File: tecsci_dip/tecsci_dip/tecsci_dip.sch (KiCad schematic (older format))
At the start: 0 parts

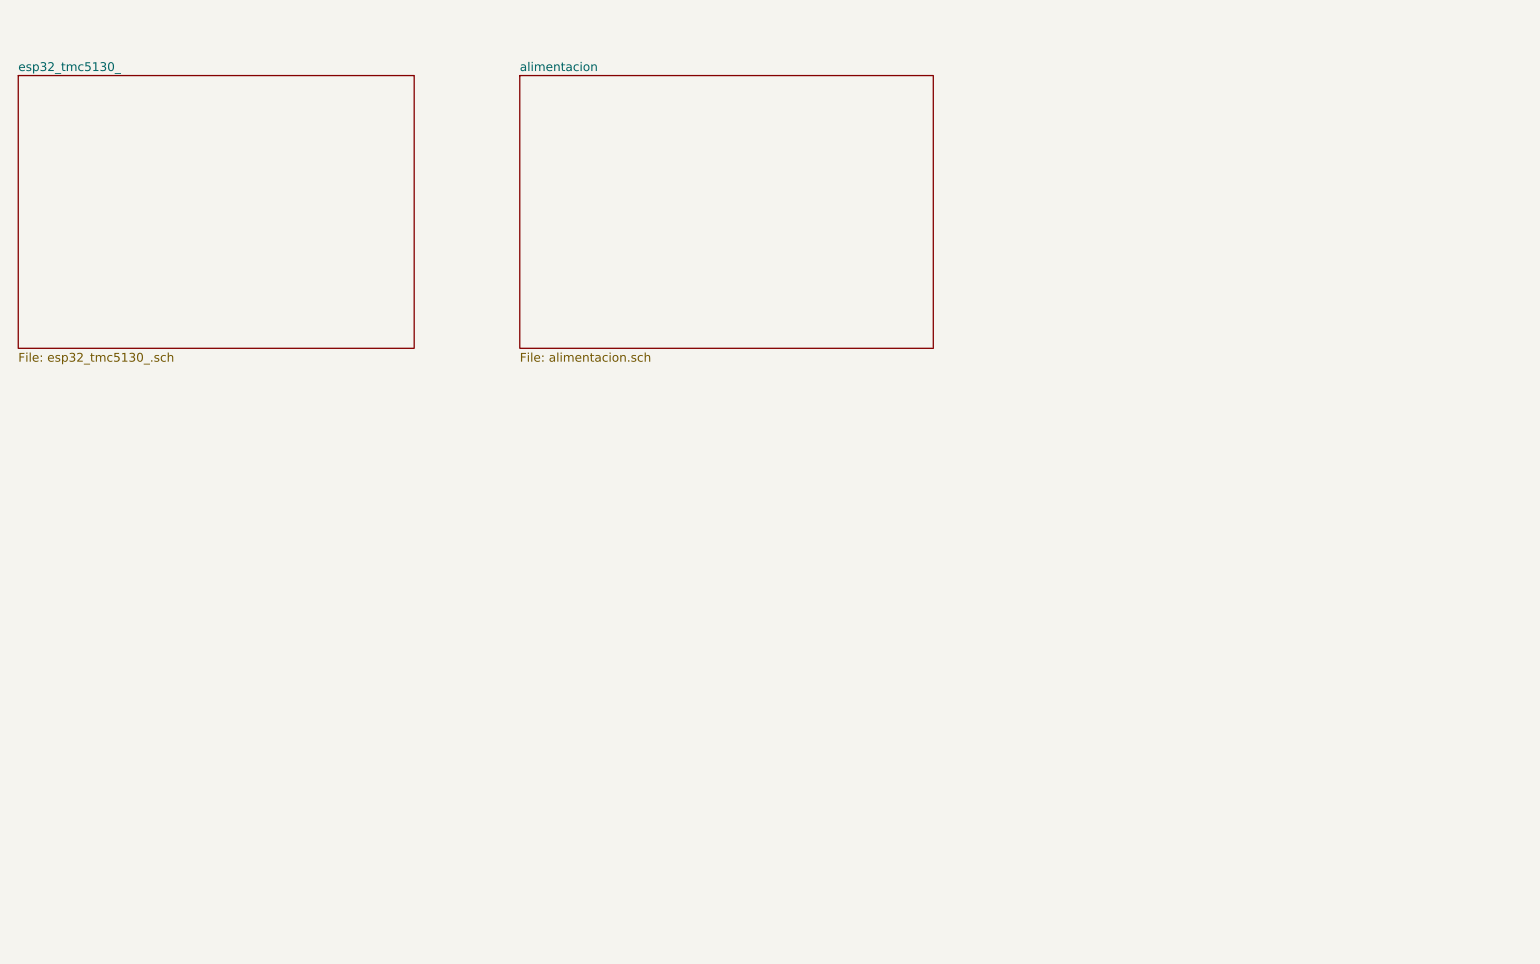
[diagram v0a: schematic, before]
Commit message: add value and footprint
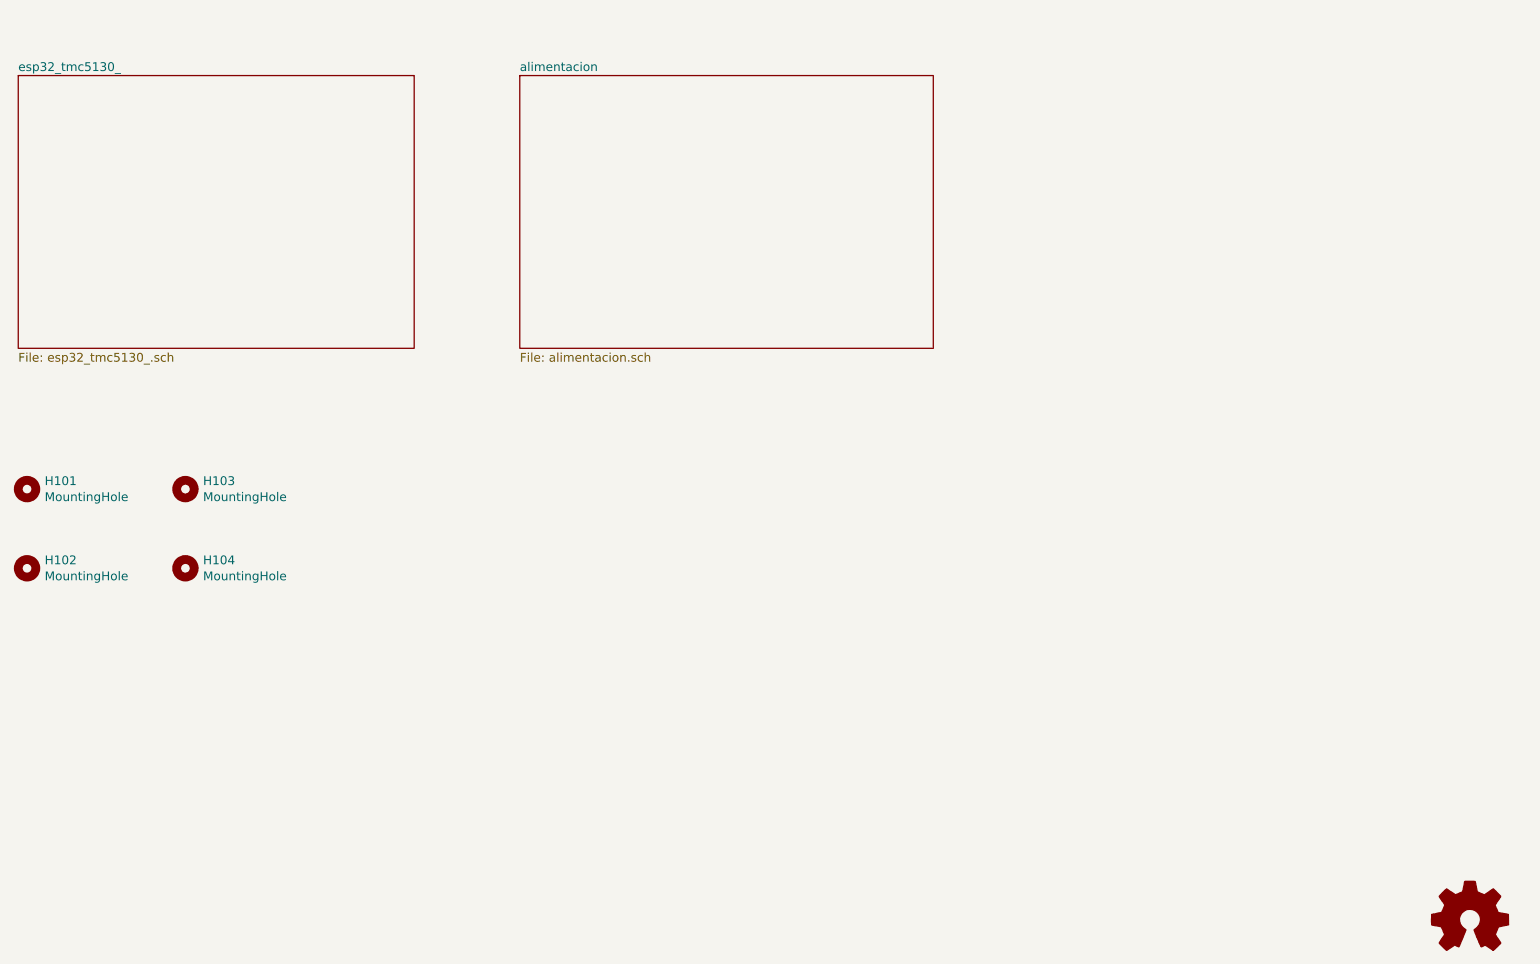
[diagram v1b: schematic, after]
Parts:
- added H101, H102, H103, H104: MountingHole, symbol Mechanical:MountingHole
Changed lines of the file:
@@
 F1 "alimentacion.sch" 50
 $EndSheet
+$Comp
+L Graphic:Logo_Open_Hardware_Small #LOGO101
+U 1 1 5DA0F2CF
+P 10650 6900
+F 0 "#LOGO101" H 10650 7175 50  0001 C CNN
+F 1 "Logo_Open_Hardware_Small" H 10650 6675 50  0001 C CNN
+F 2 "" H 10650 6900 50  0001 C CNN
+F 3 "~" H 10650 6900 50  0001 C CNN
+	1    10650 6900
+	1    0    0    -1
+$EndComp
+$Comp
+L Mechanical:MountingHole H101
+U 1 1 5DA289C8
+P 2450 4450
+F 0 "H101" H 2550 4496 50  0000 L CNN
+F 1 "MountingHole" H 2550 4405 50  0000 L CNN
+F 2 "" H 2450 4450 50  0001 C CNN
+F 3 "~" H 2450 4450 50  0001 C CNN
+	1    2450 4450
+	1    0    0    -1
+$EndComp
+$Comp
+L Mechanical:MountingHole H102
+U 1 1 5DA28E58
+P 2450 4900
+F 0 "H102" H 2550 4946 50  0000 L CNN
+F 1 "MountingHole" H 2550 4855 50  0000 L CNN
+F 2 "" H 2450 4900 50  0001 C CNN
+F 3 "~" H 2450 4900 50  0001 C CNN
+	1    2450 4900
+	1    0    0    -1
+$EndComp
+$Comp
+L Mechanical:MountingHole H103
+U 1 1 5DA28F66
+P 3350 4450
+F 0 "H103" H 3450 4496 50  0000 L CNN
+F 1 "MountingHole" H 3450 4405 50  0000 L CNN
+F 2 "" H 3350 4450 50  0001 C CNN
+F 3 "~" H 3350 4450 50  0001 C CNN
+	1    3350 4450
+	1    0    0    -1
+$EndComp
+$Comp
+L Mechanical:MountingHole H104
+U 1 1 5DA29002
+P 3350 4900
+F 0 "H104" H 3450 4946 50  0000 L CNN
+F 1 "MountingHole" H 3450 4855 50  0000 L CNN
+F 2 "" H 3350 4900 50  0001 C CNN
+F 3 "~" H 3350 4900 50  0001 C CNN
+	1    3350 4900
+	1    0    0    -1
+$EndComp
 $EndSCHEMATC

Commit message: agrego valor faltantes en esquematico
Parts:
- H101, H102, H103, H104: footprint (none) -> MountingHole:MountingHole_3mm
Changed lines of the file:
@@
 F 0 "H101" H 2550 4496 50  0000 L CNN
 F 1 "MountingHole" H 2550 4405 50  0000 L CNN
-F 2 "" H 2450 4450 50  0001 C CNN
+F 2 "MountingHole:MountingHole_3mm" H 2450 4450 50  0001 C CNN
 F 3 "~" H 2450 4450 50  0001 C CNN
 	1    2450 4450
@@
 F 0 "H102" H 2550 4946 50  0000 L CNN
 F 1 "MountingHole" H 2550 4855 50  0000 L CNN
-F 2 "" H 2450 4900 50  0001 C CNN
+F 2 "MountingHole:MountingHole_3mm" H 2450 4900 50  0001 C CNN
 F 3 "~" H 2450 4900 50  0001 C CNN
 	1    2450 4900
@@
 F 0 "H103" H 3450 4496 50  0000 L CNN
 F 1 "MountingHole" H 3450 4405 50  0000 L CNN
-F 2 "" H 3350 4450 50  0001 C CNN
+F 2 "MountingHole:MountingHole_3mm" H 3350 4450 50  0001 C CNN
 F 3 "~" H 3350 4450 50  0001 C CNN
 	1    3350 4450
@@
 F 0 "H104" H 3450 4946 50  0000 L CNN
 F 1 "MountingHole" H 3450 4855 50  0000 L CNN
-F 2 "" H 3350 4900 50  0001 C CNN
+F 2 "MountingHole:MountingHole_3mm" H 3350 4900 50  0001 C CNN
 F 3 "~" H 3350 4900 50  0001 C CNN
 	1    3350 4900

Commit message: update board
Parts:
- added OSHWA101: Logo_Open_Hardware_Small, Symbol:OSHW-Symbol_8.9x8mm_SilkScreen, symbol Graphic:Logo_Open_Hardware_Small
- H101, H102, H103, H104: footprint MountingHole:MountingHole_3mm -> MountingHole:MountingHole_3.2mm_M3_Pad_Via
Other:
- moved on the sheet: H101, H102, H103, H104
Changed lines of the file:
@@
 Date "2019-10-02"
 Rev "1"
-Comp "Tecsci"
+Comp "Tecsci  Tecnología para Ciencia"
 Comment1 "Martin Abel Gambarotta"
 Comment2 ""
-Comment3 ""
+Comment3 "Revisor: Mariano Campos"
 Comment4 ""
 $EndDescr
 $Sheet
-S 2400 2100 2250 1550
+S 2450 3850 2250 1550
 U 5D952A19
 F0 "esp32_tmc5130_" 50
@@
 $EndSheet
 $Sheet
-S 5250 2100 2350 1550
+S 2450 1850 2250 1650
 U 5D952A48
 F0 "alimentacion" 50
@@
 $EndSheet
 $Comp
-L Graphic:Logo_Open_Hardware_Small #LOGO101
-U 1 1 5DA0F2CF
-P 10650 6900
-F 0 "#LOGO101" H 10650 7175 50  0001 C CNN
-F 1 "Logo_Open_Hardware_Small" H 10650 6675 50  0001 C CNN
-F 2 "" H 10650 6900 50  0001 C CNN
-F 3 "~" H 10650 6900 50  0001 C CNN
-	1    10650 6900
-	1    0    0    -1
-$EndComp
-$Comp
 L Mechanical:MountingHole H101
 U 1 1 5DA289C8
-P 2450 4450
-F 0 "H101" H 2550 4496 50  0000 L CNN
-F 1 "MountingHole" H 2550 4405 50  0000 L CNN
-F 2 "MountingHole:MountingHole_3mm" H 2450 4450 50  0001 C CNN
-F 3 "~" H 2450 4450 50  0001 C CNN
-	1    2450 4450
+P 2550 6250
+F 0 "H101" H 2650 6296 50  0000 L CNN
+F 1 "MountingHole" H 2650 6205 50  0000 L CNN
+F 2 "MountingHole:MountingHole_3.2mm_M3_Pad_Via" H 2550 6250 50  0001 C CNN
+F 3 "~" H 2550 6250 50  0001 C CNN
+	1    2550 6250
 	1    0    0    -1
 $EndComp
@@
 L Mechanical:MountingHole H102
 U 1 1 5DA28E58
-P 2450 4900
-F 0 "H102" H 2550 4946 50  0000 L CNN
-F 1 "MountingHole" H 2550 4855 50  0000 L CNN
-F 2 "MountingHole:MountingHole_3mm" H 2450 4900 50  0001 C CNN
-F 3 "~" H 2450 4900 50  0001 C CNN
-	1    2450 4900
+P 2550 6700
+F 0 "H102" H 2650 6746 50  0000 L CNN
+F 1 "MountingHole" H 2650 6655 50  0000 L CNN
+F 2 "MountingHole:MountingHole_3.2mm_M3_Pad_Via" H 2550 6700 50  0001 C CNN
+F 3 "~" H 2550 6700 50  0001 C CNN
+	1    2550 6700
 	1    0    0    -1
 $EndComp
@@
 L Mechanical:MountingHole H103
 U 1 1 5DA28F66
-P 3350 4450
-F 0 "H103" H 3450 4496 50  0000 L CNN
-F 1 "MountingHole" H 3450 4405 50  0000 L CNN
-F 2 "MountingHole:MountingHole_3mm" H 3350 4450 50  0001 C CNN
-F 3 "~" H 3350 4450 50  0001 C CNN
-	1    3350 4450
+P 3450 6250
+F 0 "H103" H 3550 6296 50  0000 L CNN
+F 1 "MountingHole" H 3550 6205 50  0000 L CNN
+F 2 "MountingHole:MountingHole_3.2mm_M3_Pad_Via" H 3450 6250 50  0001 C CNN
+F 3 "~" H 3450 6250 50  0001 C CNN
+	1    3450 6250
 	1    0    0    -1
 $EndComp
@@
 L Mechanical:MountingHole H104
 U 1 1 5DA29002
-P 3350 4900
-F 0 "H104" H 3450 4946 50  0000 L CNN
-F 1 "MountingHole" H 3450 4855 50  0000 L CNN
-F 2 "MountingHole:MountingHole_3mm" H 3350 4900 50  0001 C CNN
-F 3 "~" H 3350 4900 50  0001 C CNN
-	1    3350 4900
+P 3450 6700
+F 0 "H104" H 3550 6746 50  0000 L CNN
+F 1 "MountingHole" H 3550 6655 50  0000 L CNN
+F 2 "MountingHole:MountingHole_3.2mm_M3_Pad_Via" H 3450 6700 50  0001 C CNN
+F 3 "~" H 3450 6700 50  0001 C CNN
+	1    3450 6700
 	1    0    0    -1
 $EndComp
+$Comp
+L Graphic:Logo_Open_Hardware_Small OSHWA101
+U 1 1 5DB645A4
+P 10750 6850
+F 0 "OSHWA101" H 10750 7125 50  0001 C CNN
+F 1 "Logo_Open_Hardware_Small" H 10750 6625 50  0001 C CNN
+F 2 "Symbol:OSHW-Symbol_8.9x8mm_SilkScreen" H 10750 6850 50  0001 C CNN
+F 3 "~" H 10750 6850 50  0001 C CNN
+	1    10750 6850
+	1    0    0    -1
+$EndComp

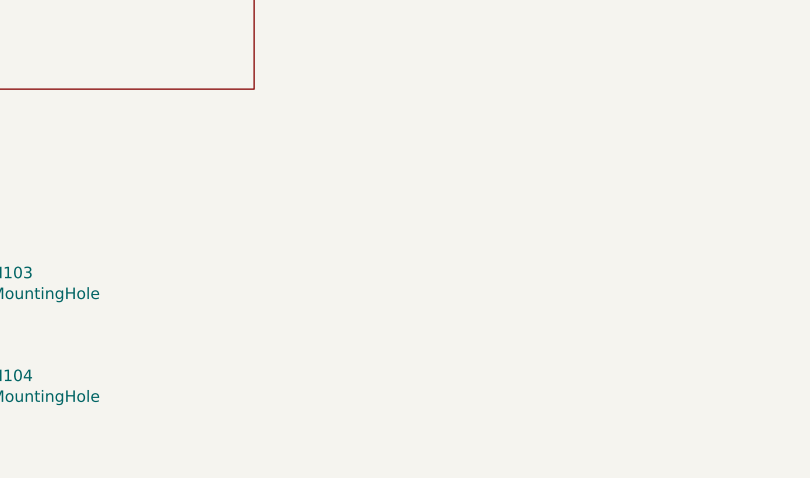
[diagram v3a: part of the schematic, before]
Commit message: add fiduciales
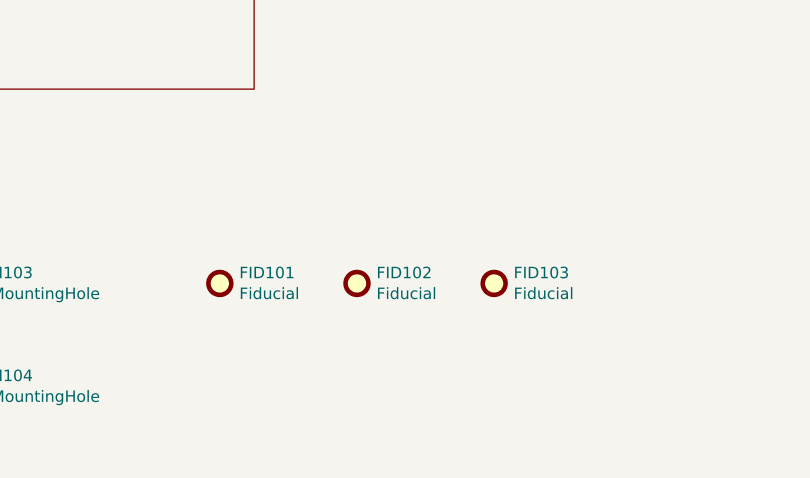
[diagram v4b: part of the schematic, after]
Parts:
- added FID101, FID102, FID103: Fiducial, Fiducial:Fiducial_1mm_Mask2mm, symbol Mechanical:Fiducial
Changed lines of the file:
@@
+	1    0    0    -1
+$EndComp
+$Comp
+L Mechanical:Fiducial FID101
+U 1 1 5DB777EA
+P 4550 6250
+F 0 "FID101" H 4635 6296 50  0000 L CNN
+F 1 "Fiducial" H 4635 6205 50  0000 L CNN
+F 2 "Fiducial:Fiducial_1mm_Mask2mm" H 4550 6250 50  0001 C CNN
+F 3 "~" H 4550 6250 50  0001 C CNN
+	1    4550 6250
+	1    0    0    -1
+$EndComp
+$Comp
+L Mechanical:Fiducial FID102
+U 1 1 5DB77DDD
+P 5150 6250
+F 0 "FID102" H 5235 6296 50  0000 L CNN
+F 1 "Fiducial" H 5235 6205 50  0000 L CNN
+F 2 "Fiducial:Fiducial_1mm_Mask2mm" H 5150 6250 50  0001 C CNN
+F 3 "~" H 5150 6250 50  0001 C CNN
+	1    5150 6250
+	1    0    0    -1
+$EndComp
+$Comp
+L Mechanical:Fiducial FID103
+U 1 1 5DB77F7E
+P 5750 6250
+F 0 "FID103" H 5835 6296 50  0000 L CNN
+F 1 "Fiducial" H 5835 6205 50  0000 L CNN
+F 2 "Fiducial:Fiducial_1mm_Mask2mm" H 5750 6250 50  0001 C CNN
+F 3 "~" H 5750 6250 50  0001 C CNN
+	1    5750 6250
 	1    0    0    -1
 $EndComp

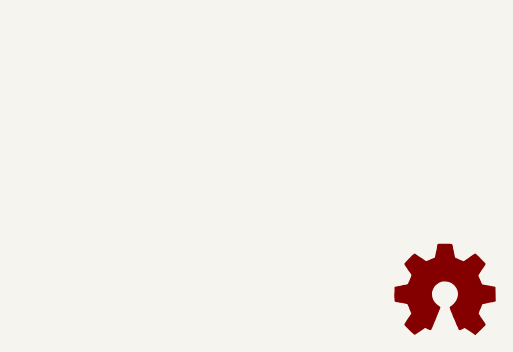
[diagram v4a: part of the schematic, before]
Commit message: Se corrigen todos los errores marcados por el profesor, excepto pasar a footprint conectores de ESP32, ya que la v2 contendra al CI
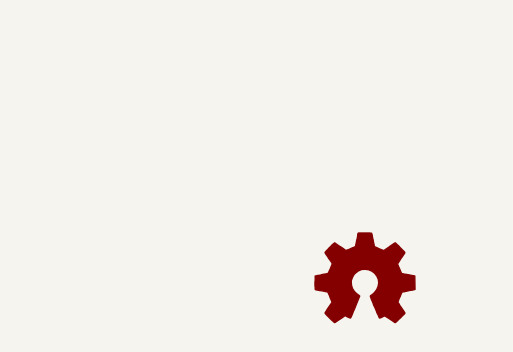
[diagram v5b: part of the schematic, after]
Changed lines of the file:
@@
 Title "Dip Coater"
 Date "2019-10-02"
-Rev "1"
-Comp "Tecsci  Tecnología para Ciencia"
-Comment1 "Martin Abel Gambarotta"
+Rev "2"
+Comp "Tecsci  Tecnología para Ciencia                            Licensed under CERN OHL v.1.2"
+Comment1 "Ing. Electrónico Martin Abel Gambarotta"
 Comment2 ""
 Comment3 "Revisor: Mariano Campos"
-Comment4 ""
+Comment4 "Revisor: Diego Brengi"
 $EndDescr
 $Sheet
@@
 L Graphic:Logo_Open_Hardware_Small OSHWA101
 U 1 1 5DB645A4
-P 10750 6850
-F 0 "OSHWA101" H 10750 7125 50  0001 C CNN
-F 1 "Logo_Open_Hardware_Small" H 10750 6625 50  0001 C CNN
-F 2 "Symbol:OSHW-Symbol_8.9x8mm_SilkScreen" H 10750 6850 50  0001 C CNN
-F 3 "~" H 10750 6850 50  0001 C CNN
-	1    10750 6850
+P 10400 6800
+F 0 "OSHWA101" H 10400 7075 50  0001 C CNN
+F 1 "Logo_Open_Hardware_Small" H 10400 6575 50  0001 C CNN
+F 2 "Symbol:OSHW-Symbol_8.9x8mm_SilkScreen" H 10400 6800 50  0001 C CNN
+F 3 "~" H 10400 6800 50  0001 C CNN
+	1    10400 6800
 	1    0    0    -1
 $EndComp
